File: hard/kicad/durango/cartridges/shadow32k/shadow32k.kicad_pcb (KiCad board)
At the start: 2 copper layers, 81.3 x 63.5 mm, 12 parts, among them J1 to Computer, J2 SD Interface, U1 27/28C256, U2 62256, U4 74HC174, U5 74HC139, U6 74HC245, U7 74HC139

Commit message: preliminary routing of shadowRAM
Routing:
- net /~OE: track 8.89 -> 57.3 mm, vias 0 -> 3
- net +5V: track 128.2 -> 130.5 mm
- net A5: track 76.2 -> 75.5 mm
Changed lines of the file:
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@@
     (thickness 1.6)
     (drawings 41)
-    (tracks 584)
+    (tracks 608)
     (zones 0)
     (modules 12)
@@
   (segment (start 85.09 93.98) (end 83.82 93.98) (width 0.25) (layer B.Cu) (net 2))
   (segment (start 64.77 97.79) (end 55.88 97.79) (width 0.25) (layer F.Cu) (net 3))
+  (segment (start 64.77 97.79) (end 66.04 97.79) (width 0.25) (layer F.Cu) (net 3))
+  (segment (start 69.363231 96.664999) (end 70.488232 97.79) (width 0.25) (layer F.Cu) (net 3))
+  (segment (start 67.165001 96.664999) (end 69.363231 96.664999) (width 0.25) (layer F.Cu) (net 3))
+  (segment (start 66.04 97.79) (end 67.165001 96.664999) (width 0.25) (layer F.Cu) (net 3))
+  (segment (start 70.488232 97.79) (end 76.2 97.79) (width 0.25) (layer F.Cu) (net 3))
+  (segment (start 76.290001 102.583001) (end 76.290001 106.135001) (width 0.25) (layer F.Cu) (net 3))
+  (segment (start 76.925001 101.251999) (end 76.925001 101.948001) (width 0.25) (layer F.Cu) (net 3))
+  (segment (start 76.2 100.526998) (end 76.925001 101.251999) (width 0.25) (layer F.Cu) (net 3))
+  (via (at 76.835 106.68) (size 0.8) (drill 0.4) (layers F.Cu B.Cu) (net 3))
+  (segment (start 76.925001 101.948001) (end 76.290001 102.583001) (width 0.25) (layer F.Cu) (net 3))
+  (segment (start 76.290001 106.135001) (end 76.835 106.68) (width 0.25) (layer F.Cu) (net 3))
+  (segment (start 76.2 97.79) (end 76.2 100.526998) (width 0.25) (layer F.Cu) (net 3))
+  (via (at 95.25 113.03) (size 0.8) (drill 0.4) (layers F.Cu B.Cu) (net 3))
+  (segment (start 99.06 113.03) (end 95.25 113.03) (width 0.25) (layer B.Cu) (net 3))
+  (via (at 93.98 109.22) (size 0.8) (drill 0.4) (layers F.Cu B.Cu) (net 3))
+  (segment (start 95.25 110.49) (end 93.98 109.22) (width 0.25) (layer F.Cu) (net 3))
+  (segment (start 95.25 113.03) (end 95.25 110.49) (width 0.25) (layer F.Cu) (net 3))
+  (segment (start 91.44 106.68) (end 76.835 106.68) (width 0.25) (layer B.Cu) (net 3))
+  (segment (start 93.98 109.22) (end 91.44 106.68) (width 0.25) (layer B.Cu) (net 3))
   (segment (start 68.58 110.49) (end 68.58 113.03) (width 0.4) (layer F.Cu) (net 4))
   (segment (start 68.58 113.03) (end 71.12 113.03) (width 0.4) (layer F.Cu) (net 4))
   (segment (start 68.58 113.03) (end 55.88 113.03) (width 0.4) (layer F.Cu) (net 4))
   (segment (start 71.12 113.03) (end 71.755 113.03) (width 0.4) (layer F.Cu) (net 4))
-  (segment (start 71.755 113.03) (end 72.39 113.03) (width 0.4) (layer F.Cu) (net 4))
-  (segment (start 72.39 113.03) (end 83.82 113.03) (width 0.4) (layer F.Cu) (net 4))
   (segment (start 71.55 112.825) (end 71.755 113.03) (width 0.4) (layer F.Cu) (net 4))
   (segment (start 71.55 104.775) (end 71.55 112.825) (width 0.4) (layer F.Cu) (net 4))
@@
   (segment (start 116.84 85.09) (end 114.3 82.55) (width 0.4) (layer B.Cu) (net 4))
   (segment (start 110.49 110.49) (end 115.65 110.49) (width 0.4) (layer B.Cu) (net 4))
+  (segment (start 83.82 114.3) (end 83.82 113.03) (width 0.4) (layer F.Cu) (net 4))
+  (segment (start 74.295 114.935) (end 83.185 114.935) (width 0.4) (layer F.Cu) (net 4))
+  (segment (start 72.39 113.03) (end 74.295 114.935) (width 0.4) (layer F.Cu) (net 4))
+  (segment (start 83.185 114.935) (end 83.82 114.3) (width 0.4) (layer F.Cu) (net 4))
+  (segment (start 71.755 113.03) (end 72.39 113.03) (width 0.4) (layer F.Cu) (net 4))
   (segment (start 85.07 82.55) (end 83.82 82.55) (width 0.25) (layer B.Cu) (net 5))
   (segment (start 71.12 82.55) (end 69.85 81.28) (width 0.25) (layer B.Cu) (net 5))
@@
   (segment (start 83.82 102.87) (end 71.12 102.87) (width 0.25) (layer B.Cu) (net 13))
   (segment (start 71.12 102.87) (end 69.85 101.6) (width 0.25) (layer B.Cu) (net 13))
-  (segment (start 80.85 99.695) (end 79.375 99.695) (width 0.25) (layer F.Cu) (net 13))
-  (via (at 77.199999 102.928023) (size 0.8) (drill 0.4) (layers F.Cu B.Cu) (net 13))
-  (segment (start 77.199999 101.870001) (end 77.199999 102.928023) (width 0.25) (layer F.Cu) (net 13))
-  (segment (start 79.375 99.695) (end 77.199999 101.870001) (width 0.25) (layer F.Cu) (net 13))
   (segment (start 69.85 101.6) (end 67.31 101.6) (width 0.25) (layer B.Cu) (net 13))
   (segment (start 67.31 101.6) (end 66.04 102.87) (width 0.25) (layer B.Cu) (net 13))
@@
   (segment (start 86.995 114.3) (end 105.41 114.3) (width 0.25) (layer B.Cu) (net 13))
   (via (at 86.995 114.3) (size 0.8) (drill 0.4) (layers F.Cu B.Cu) (net 13))
+  (segment (start 80.47929 100.06571) (end 79.98788 100.06571) (width 0.25) (layer F.Cu) (net 13))
+  (segment (start 80.85 99.695) (end 80.47929 100.06571) (width 0.25) (layer F.Cu) (net 13))
+  (via (at 77.199999 102.87) (size 0.8) (drill 0.4) (layers F.Cu B.Cu) (net 13))
+  (segment (start 77.199999 102.853591) (end 77.199999 102.87) (width 0.25) (layer F.Cu) (net 13))
+  (segment (start 79.98788 100.06571) (end 77.199999 102.853591) (width 0.25) (layer F.Cu) (net 13))
   (segment (start 83.82 105.41) (end 71.12 105.41) (width 0.25) (layer B.Cu) (net 14))
   (segment (start 71.12 105.41) (end 69.85 104.14) (width 0.25) (layer B.Cu) (net 14))
@@
   (segment (start 86.36 113.03) (end 91.44 113.03) (width 0.25) (layer B.Cu) (net 17))
   (segment (start 100.965 113.03) (end 102.87 113.03) (width 0.25) (layer B.Cu) (net 17))
-  (segment (start 98.519999 111.904999) (end 99.839999 111.904999) (width 0.25) (layer B.Cu) (net 17))
-  (segment (start 97.394998 113.03) (end 98.519999 111.904999) (width 0.25) (layer B.Cu) (net 17))
-  (segment (start 99.839999 111.904999) (end 100.965 113.03) (width 0.25) (layer B.Cu) (net 17))
-  (segment (start 91.44 113.03) (end 97.394998 113.03) (width 0.25) (layer B.Cu) (net 17))
+  (segment (start 99.695 111.76) (end 100.965 113.03) (width 0.25) (layer B.Cu) (net 17))
+  (segment (start 92.71 111.76) (end 99.695 111.76) (width 0.25) (layer B.Cu) (net 17))
+  (segment (start 91.44 113.03) (end 92.71 111.76) (width 0.25) (layer B.Cu) (net 17))
   (segment (start 102.87 74.295) (end 102.87 77.47) (width 0.25) (layer B.Cu) (net 18))
   (via (at 62.865 75.565) (size 0.8) (drill 0.4) (layers F.Cu B.Cu) (net 18))
@@
   (segment (start 85.09 121.92) (end 85.09 99.695) (width 0.25) (layer F.Cu) (net 35))
   (segment (start 74.660003 96.592999) (end 74.660003 96.52) (width 0.25) (layer F.Cu) (net 36))
-  (segment (start 73.727292 97.52571) (end 74.660003 96.592999) (width 0.25) (layer F.Cu) (net 36))
   (via (at 74.660003 96.52) (size 0.8) (drill 0.4) (layers F.Cu B.Cu) (net 36))
-  (segment (start 71.92071 97.52571) (end 73.727292 97.52571) (width 0.25) (layer F.Cu) (net 36))
-  (segment (start 71.55 97.155) (end 71.92071 97.52571) (width 0.25) (layer F.Cu) (net 36))
   (segment (start 74.660003 96.52) (end 85.09 96.52) (width 0.25) (layer B.Cu) (net 36))
   (segment (start 85.09 96.52) (end 85.725 96.52) (width 0.25) (layer B.Cu) (net 36))
@@
   (segment (start 97.79 127) (end 99.06 128.27) (width 0.25) (layer B.Cu) (net 36))
   (segment (start 86.36 127) (end 97.79 127) (width 0.25) (layer B.Cu) (net 36))
+  (segment (start 74.660003 97.085685) (end 74.660003 96.52) (width 0.25) (layer F.Cu) (net 36))
+  (segment (start 74.500687 97.245001) (end 74.660003 97.085685) (width 0.25) (layer F.Cu) (net 36))
+  (segment (start 73.221998 97.155) (end 73.311999 97.245001) (width 0.25) (layer F.Cu) (net 36))
+  (segment (start 73.311999 97.245001) (end 74.500687 97.245001) (width 0.25) (layer F.Cu) (net 36))
+  (segment (start 71.55 97.155) (end 73.221998 97.155) (width 0.25) (layer F.Cu) (net 36))
   (segment (start 99.859999 117.310001) (end 99.06 118.11) (width 0.25) (layer F.Cu) (net 37))
   (segment (start 100.235001 116.934999) (end 99.859999 117.310001) (width 0.25) (layer F.Cu) (net 37))

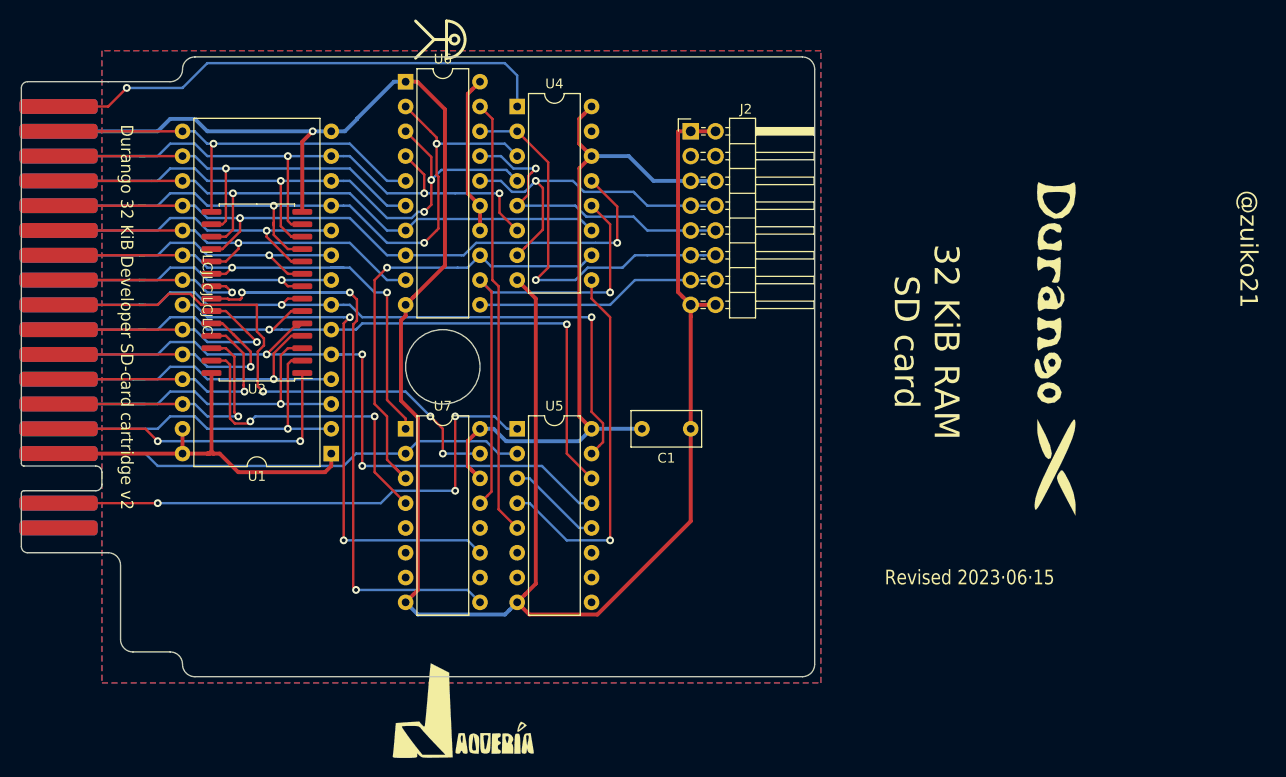
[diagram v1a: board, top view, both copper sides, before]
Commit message: alternative routing in ShadowRAM
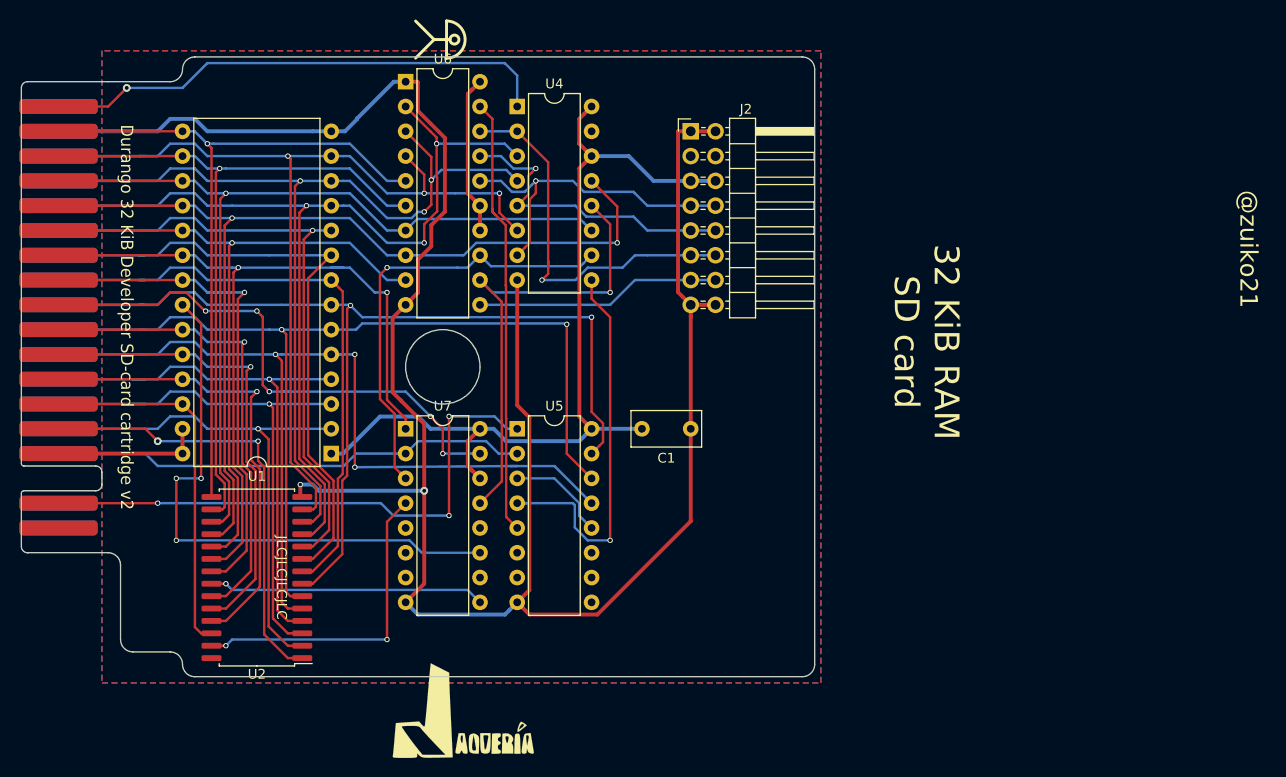
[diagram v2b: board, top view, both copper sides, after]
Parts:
- removed LOGO1: Logo_Open_Hardware_Large, Symbol:OSHW-Logo2_24.3x20mm_SilkScreen
- removed LOGO3: Logo_Open_Hardware_Small, durango:durango-x90
- moved U2 29.2 mm to (76.2, 125.7)
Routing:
- net /RAM~OE: track 70.2 -> 28.5 mm, vias 3 -> 1
- net A10: track 20.7 -> 53.7 mm
- net D2: track 65.9 -> 96.2 mm
- net D1: track 67.0 -> 97.3 mm
- net A2: track 32.0 -> 62.3 mm, vias 1 -> 0
- net A0: track 35.0 -> 65.2 mm
- net /~CS: track 53.6 -> 83.9 mm
- net A1: track 34.7 -> 64.7 mm, vias 1 -> 0
- net D7: track 41.6 -> 71.3 mm
- net D0: track 72.3 -> 102.0 mm
- net D4: track 44.6 -> 74.3 mm
- net D6: track 72.4 -> 102.0 mm
- net D5: track 63.9 -> 93.3 mm
- net D3: track 44.7 -> 74.0 mm
- net A3: track 74.1 -> 102.9 mm
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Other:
- board text removed: "Revised 2023·06·15"
- board text removed: "Serial No."

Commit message: definitive silkscreen on ShadowRAM
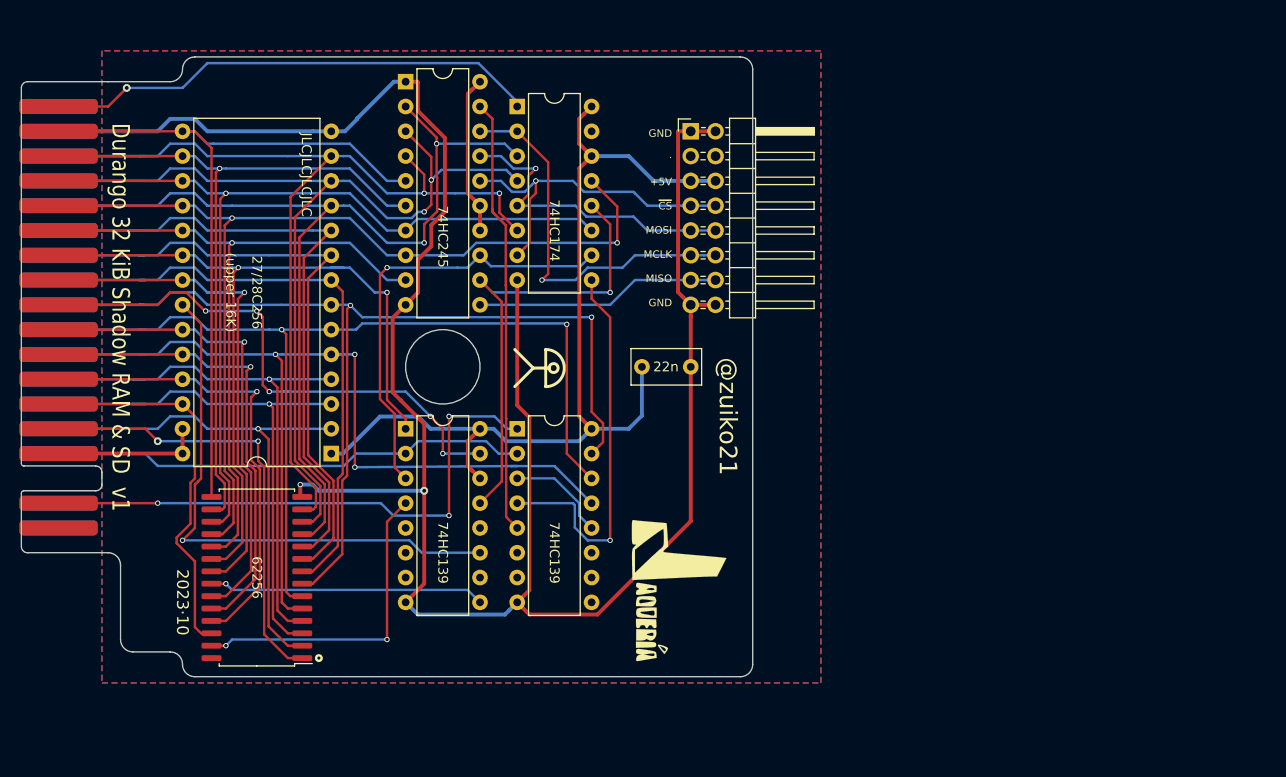
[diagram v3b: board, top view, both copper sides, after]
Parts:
- moved LOGO2 25.4 mm to (119.4, 127.0), turned to 270 degrees
- moved C1 6.35 mm to (120.7, 104.1)
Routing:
- net +5V: track 121.5 -> 127.0 mm
- net D3: track 74.0 -> 77.1 mm, vias 1 -> 0
- net /ROM~OE: track 59.1 -> 56.7 mm, vias 3 -> 1
- net D2: track 96.2 -> 97.8 mm, vias 3 -> 2
- net /~RST: track 52.5 -> 50.9 mm
- net A13: track 38.0 -> 39.6 mm
- net D1: track 97.3 -> 98.6 mm, vias 3 -> 2
- net D0: track 102.0 -> 103.0 mm, vias 3 -> 2
- net A0: track 65.2 -> 66.0 mm, vias 1 -> 0
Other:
- board size 81.3 x 63.5 mm -> 74.9 x 63.5 mm
- board text added: "(upper 16K)"
- board text added: "2023·10"
- board text added: "Durango 32 KiB Shadow RAM & SD v1"
- board text added: "GND · +5V ~CS~ MOSI MCLK MISO GND"
- board text removed: "32 KiB RAM SD card"
- board text removed: "Durango 32 KiB Developer SD-card cartridge v2"

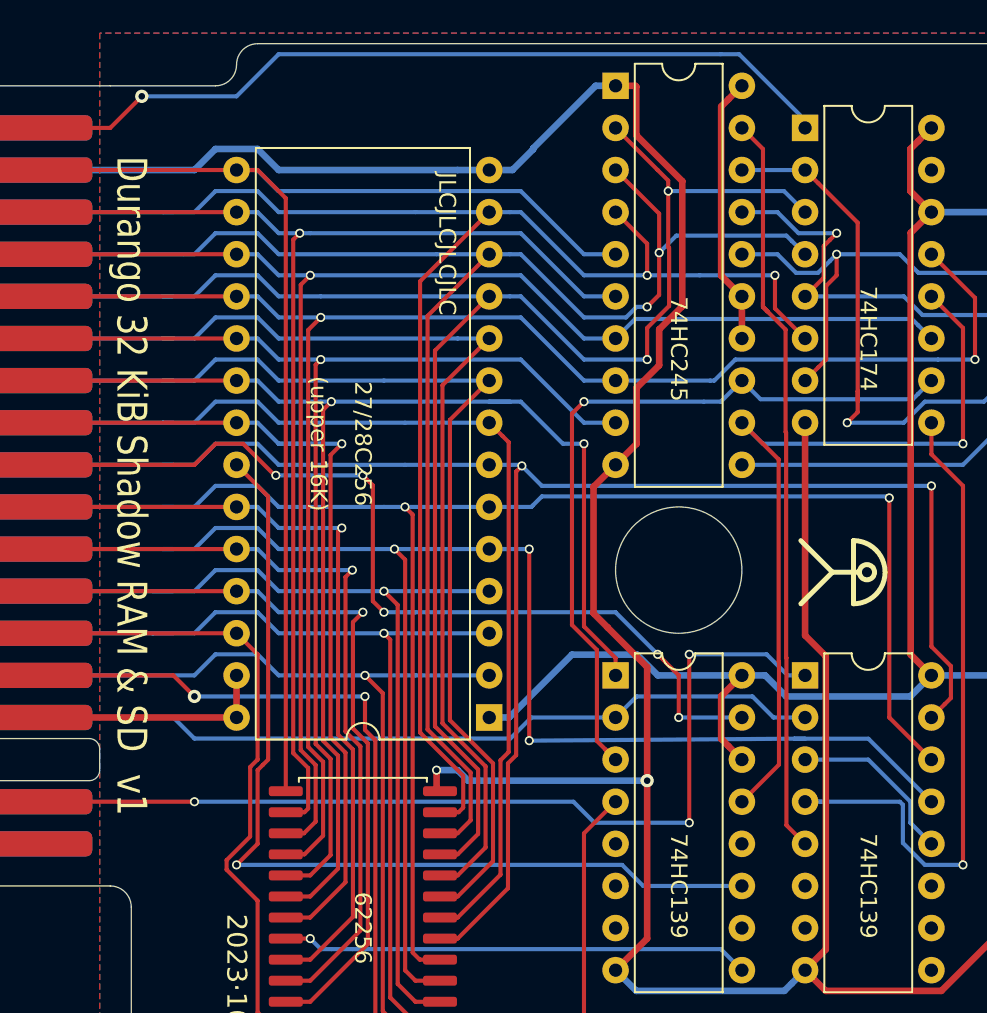
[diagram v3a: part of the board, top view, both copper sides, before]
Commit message: improved silkscreen
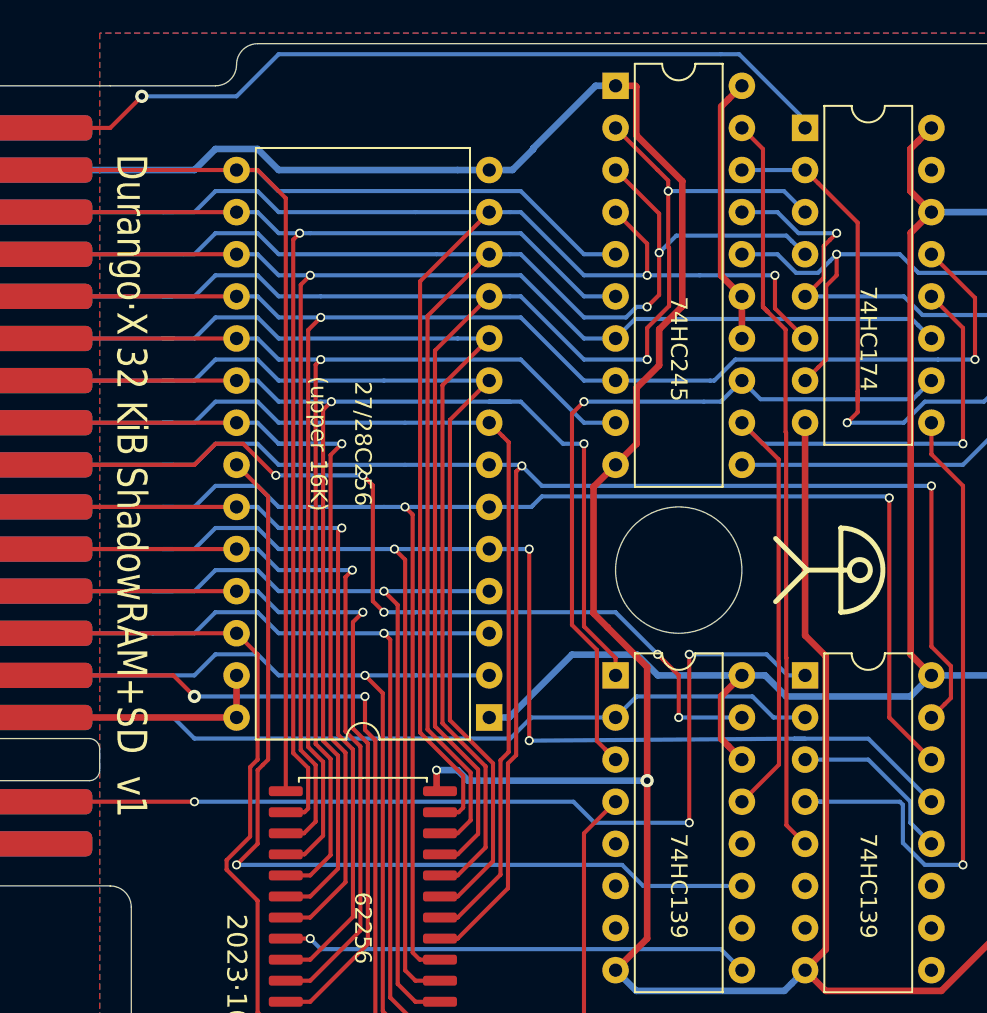
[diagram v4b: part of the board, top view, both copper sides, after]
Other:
- board text added: "Durango·X 32 KiB ShadowRAM+SD v1"
- board text removed: "Durango 32 KiB Shadow RAM & SD v1"
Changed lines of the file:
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@@
   (general
     (thickness 1.6)
-    (drawings 41)
+    (drawings 42)
     (tracks 681)
     (zones 0)
@@
     (pad 1 smd roundrect (at 45.72 -3.81 270) (size 1.524 8) (layers F.Cu F.Paste F.Mask) (roundrect_rratio 0.25))
   )
+  (gr_text "GND\n\n ·\n\n+5V\n\n~CS~\n\nMOSI\n\nMCLK\n\nMISO\n\nGND" (at 118.745 88.9) (layer B.SilkS)
+    (effects (font (size 0.77 0.77) (thickness 0.15)) (justify left mirror))
+  )
   (gr_text "GND\n\n ·\n\n+5V\n\n~CS~\n\nMOSI\n\nMCLK\n\nMISO\n\nGND" (at 118.745 88.9) (layer F.SilkS)
     (effects (font (size 0.77 0.77) (thickness 0.15)) (justify right))
@@
   (gr_arc (start 52.705 75.565) (end 52.705 74.93) (angle -90) (layer Edge.Cuts) (width 0.05))
   (gr_line (start 60.96 74.93) (end 52.705 74.93) (layer Edge.Cuts) (width 0.05))
-  (gr_line (start 104.521 104.267) (end 102.616 106.172) (layer F.SilkS) (width 0.3))
-  (gr_line (start 104.521 104.267) (end 102.616 102.362) (layer F.SilkS) (width 0.3))
-  (gr_line (start 106.14519 104.267) (end 104.521 104.267) (layer F.SilkS) (width 0.3))
-  (gr_line (start 105.791 102.362) (end 105.791 106.172) (layer F.SilkS) (width 0.3))
-  (gr_circle (center 106.603095 104.267) (end 107.061 104.267) (layer F.SilkS) (width 0.3))
-  (gr_arc (start 105.791 104.267) (end 105.791 106.172) (angle -180) (layer F.SilkS) (width 0.3))
+  (gr_line (start 102.997 104.14) (end 101.092 106.045) (layer F.SilkS) (width 0.3))
+  (gr_line (start 102.997 104.14) (end 101.092 102.235) (layer F.SilkS) (width 0.3))
+  (gr_line (start 105.537 104.14) (end 102.997 104.14) (layer F.SilkS) (width 0.3))
+  (gr_line (start 105.029 101.6) (end 105.029 106.68) (layer F.SilkS) (width 0.3))
+  (gr_circle (center 106.172 104.14) (end 106.807 104.14) (layer F.SilkS) (width 0.3))
+  (gr_arc (start 105.029 104.14) (end 105.029 106.68) (angle -180) (layer F.SilkS) (width 0.3))
   (gr_arc (start 125.73 134.62) (end 125.73 135.89) (angle -90) (layer Edge.Cuts) (width 0.05))
   (gr_line (start 127 134.62) (end 127 73.66) (layer Edge.Cuts) (width 0.05))
   (gr_line (start 69.85 135.89) (end 125.73 135.89) (layer Edge.Cuts) (width 0.05))
   (gr_arc (start 125.73 73.66) (end 127 73.66) (angle -90) (layer Edge.Cuts) (width 0.05))
-  (gr_text JLCJLCJLCJLC (at 81.28 84.455 270) (layer F.SilkS)
-    (effects (font (size 1.016 1.016) (thickness 0.1575)))
+  (gr_text JLCJLCJLCJLC (at 96.52 132.08) (layer B.SilkS)
+    (effects (font (size 1.016 1.016) (thickness 0.1575)) (justify mirror))
   )
   (gr_text @zuiko21 (at 124.46 109.22 270) (layer F.SilkS)
     (effects (font (size 1.8 1.8) (thickness 0.4)))
   )
-  (gr_text "Durango 32 KiB Shadow RAM & SD  v1" (at 62.23 99.06 270) (layer F.SilkS)
+  (gr_text "Durango·X 32 KiB ShadowRAM+SD  v1" (at 62.23 99.06 270) (layer F.SilkS)
     (effects (font (size 1.8 1.5) (thickness 0.3)))
   )
